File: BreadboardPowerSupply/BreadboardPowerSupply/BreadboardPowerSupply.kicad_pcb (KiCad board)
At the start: 2 copper layers, 30.5 x 52.1 mm, 15 parts, among them J1 Barrel_Jack_Switch, J2 Conn_02x02_Odd_Even, J3 Conn_02x02_Odd_Even, SW1 SW_DPDT_x2, U1 LM7805_TO220

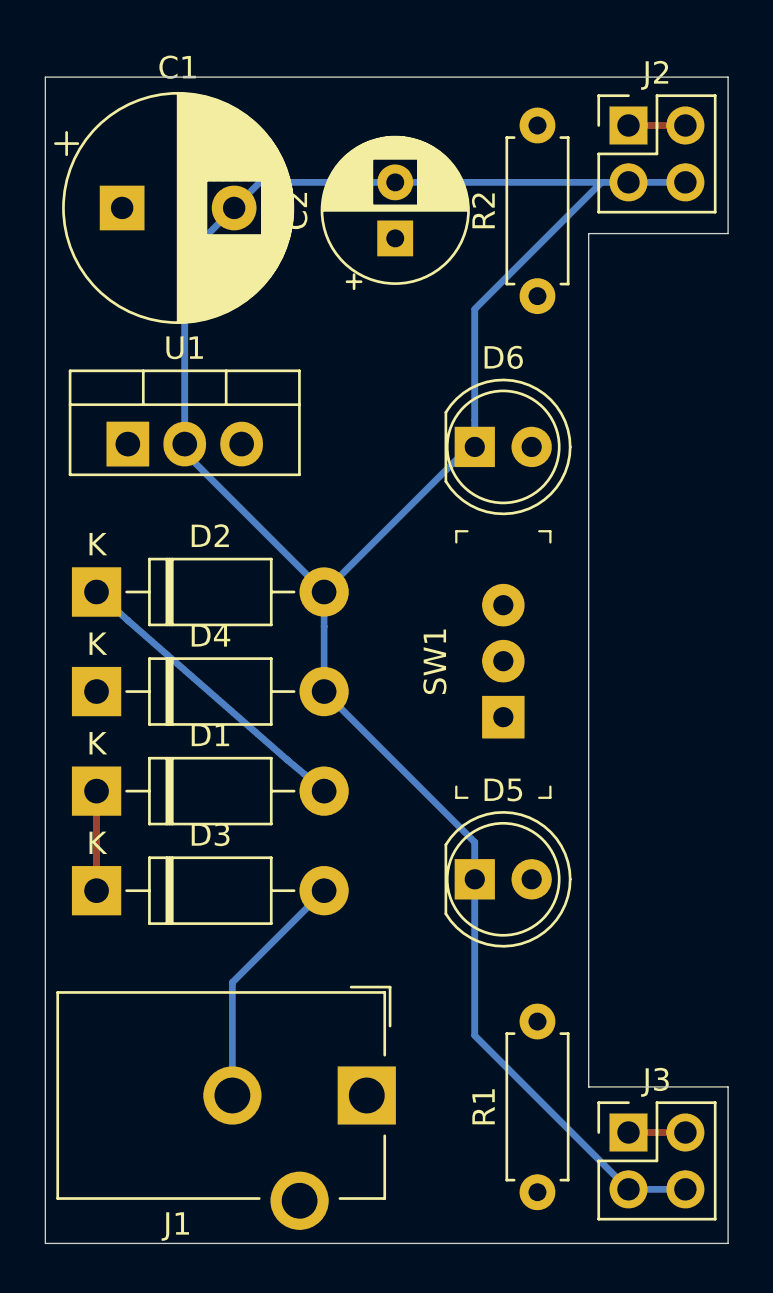
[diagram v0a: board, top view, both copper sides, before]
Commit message: start on raspberry pi hat
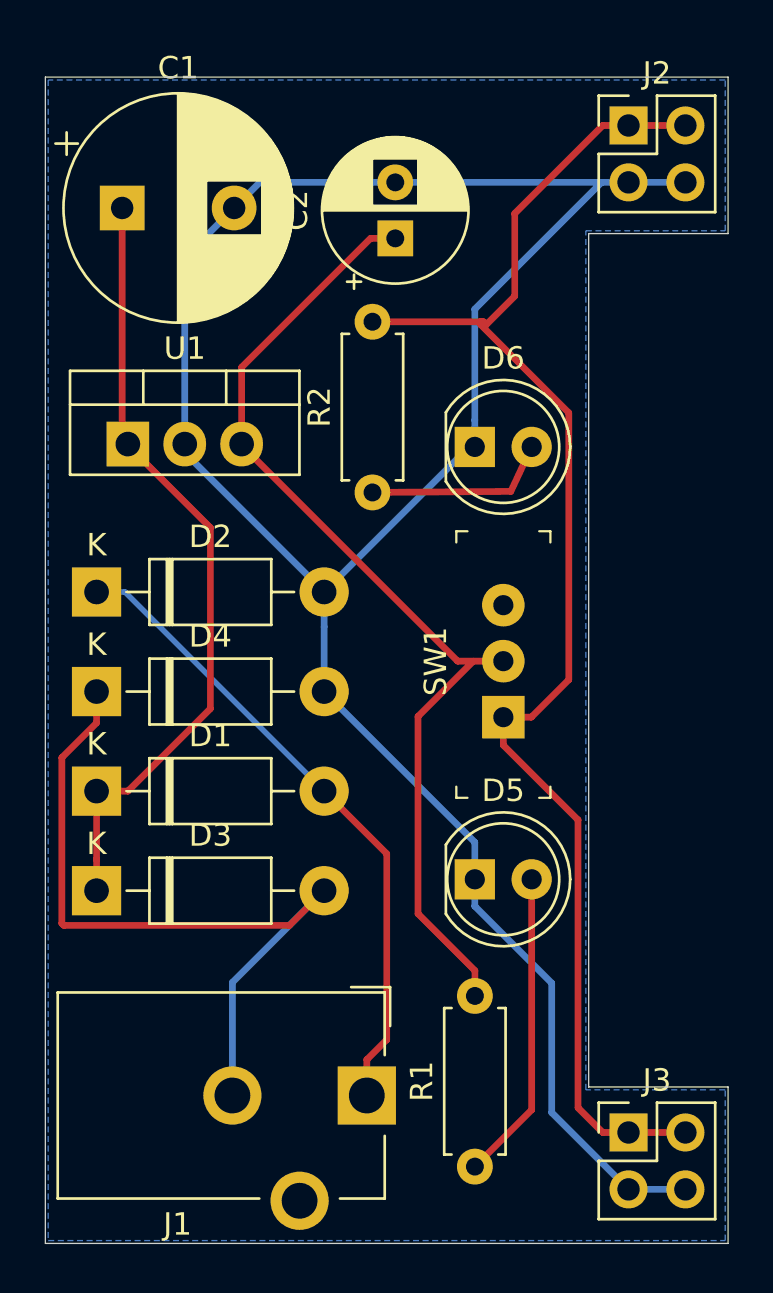
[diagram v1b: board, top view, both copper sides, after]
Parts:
- moved R2 11.4 mm to (141.2, 86.4)
- moved R1 3.02 mm to (145.8, 116.5)
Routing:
- net /Vout2: track 5.08 -> 65.2 mm
- net /Vout1: track 0.00 -> 45.4 mm
- net /Vin: track 4.45 -> 35.0 mm
- net Net-(D3-Pad2): track 10.8 -> 34.2 mm
- net Net-(D1-Pad2): track 13.5 -> 29.0 mm
- net Net-(D5-Pad2): track 0.00 -> 13.9 mm
- net Net-(D6-Pad2): track 0.00 -> 8.37 mm
- added copper zone on B.Cu, net /V-
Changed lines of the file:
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@@
     (thickness 1.6)
     (drawings 33)
-    (tracks 31)
+    (tracks 80)
     (zones 0)
     (modules 15)
@@
   )
   (setup
-    (last_trace_width 0.3)
+    (last_trace_width 0.25)
     (user_trace_width 0.3)
     (trace_clearance 0.2)
@@
     (uvia_dia 0.3)
     (uvia_drill 0.1)
-    (add_net "Net-(D1-Pad2)")
-    (add_net "Net-(D5-Pad2)")
-    (add_net "Net-(D6-Pad2)")
-    (add_net "Net-(J1-Pad3)")
-    (add_net "Net-(SW1-Pad3)")
   )
   (net_class Power ""
@@
     (add_net /Vout1)
     (add_net /Vout2)
+    (add_net "Net-(D1-Pad2)")
     (add_net "Net-(D3-Pad2)")
+    (add_net "Net-(D5-Pad2)")
+    (add_net "Net-(D6-Pad2)")
+    (add_net "Net-(J1-Pad3)")
+    (add_net "Net-(SW1-Pad3)")
   )
   (module Capacitor_THT:CP_Radial_D6.3mm_P2.50mm (layer F.Cu)
@@
   )
   (module Resistor_THT:R_Axial_DIN0207_L6.3mm_D2.5mm_P7.62mm_Horizontal (layer F.Cu)
-    (at 148.59 117.602 90)
+    (at 145.796 116.459 90)
     (descr "Resistor, Axial_DIN0207 series, Axial, Horizontal, pin pitch=7.62mm, 0.25W = 1/4W, length*diameter=6.3*2.5mm^2, http://cdn-reichelt.de/documents/datenblatt/B400/1_4W%23YAG.pdf")
     (tags "Resistor Axial_DIN0207 series Axial Horizontal pin pitch 7.62mm 0.25W = 1/4W length 6.3mm diameter 2.5mm")
@@
   )
   (module Resistor_THT:R_Axial_DIN0207_L6.3mm_D2.5mm_P7.62mm_Horizontal (layer F.Cu)
-    (at 148.59 77.597 90)
+    (at 141.224 86.36 90)
     (descr "Resistor, Axial_DIN0207 series, Axial, Horizontal, pin pitch=7.62mm, 0.25W = 1/4W, length*diameter=6.3*2.5mm^2, http://cdn-reichelt.de/documents/datenblatt/B400/1_4W%23YAG.pdf")
     (tags "Resistor Axial_DIN0207 series Axial Horizontal pin pitch 7.62mm 0.25W = 1/4W length 6.3mm diameter 2.5mm")
@@
   (segment (start 128.905 102.74) (end 128.905 99.695) (width 0.3) (layer F.Cu) (net 1))
   (segment (start 128.905 104.14) (end 128.905 102.74) (width 0.3) (layer F.Cu) (net 1))
+  (segment (start 130.305 99.695) (end 133.988 96.012) (width 0.3) (layer F.Cu) (net 1))
+  (segment (start 128.905 99.695) (end 130.305 99.695) (width 0.3) (layer F.Cu) (net 1))
+  (segment (start 130.302 84.2485) (end 130.302 84.201) (width 0.3) (layer F.Cu) (net 1))
+  (segment (start 133.988 87.9345) (end 130.302 84.2485) (width 0.3) (layer F.Cu) (net 1))
+  (segment (start 133.988 96.012) (end 133.988 87.9345) (width 0.3) (layer F.Cu) (net 1))
+  (segment (start 130.048 83.947) (end 130.302 84.201) (width 0.3) (layer F.Cu) (net 1))
+  (segment (start 130.048 73.66) (end 130.048 83.947) (width 0.3) (layer F.Cu) (net 1))
   (segment (start 155.194 117.475) (end 152.654 117.475) (width 0.3) (layer B.Cu) (net 2))
-  (segment (start 145.791 110.612) (end 145.791 103.632) (width 0.3) (layer B.Cu) (net 2))
-  (segment (start 152.654 117.475) (end 145.791 110.612) (width 0.3) (layer B.Cu) (net 2))
   (segment (start 155.194 72.517) (end 152.654 72.517) (width 0.3) (layer B.Cu) (net 2))
   (segment (start 145.791 83.128) (end 145.791 84.328) (width 0.3) (layer B.Cu) (net 2))
@@
   (segment (start 136.191 72.517) (end 142.24 72.517) (width 0.3) (layer B.Cu) (net 2))
   (segment (start 135.048 73.66) (end 136.191 72.517) (width 0.3) (layer B.Cu) (net 2))
-  (segment (start 138.176 98.933) (end 139.065 99.695) (width 0.3) (layer B.Cu) (net 4))
-  (segment (start 137.414 98.298) (end 138.176 98.933) (width 0.3) (layer B.Cu) (net 4))
-  (segment (start 128.905 90.805) (end 130.302 92.075) (width 0.3) (layer B.Cu) (net 4))
-  (segment (start 130.302 92.075) (end 137.414 98.298) (width 0.3) (layer B.Cu) (net 4))
+  (segment (start 145.791 104.832) (end 149.225 108.266) (width 0.3) (layer B.Cu) (net 2))
+  (segment (start 145.791 103.632) (end 145.791 104.832) (width 0.3) (layer B.Cu) (net 2))
+  (segment (start 149.225 114.046) (end 152.654 117.475) (width 0.3) (layer B.Cu) (net 2))
+  (segment (start 149.225 108.266) (end 149.225 114.046) (width 0.3) (layer B.Cu) (net 2))
+  (segment (start 145.796 107.70763) (end 143.256 105.16763) (width 0.3) (layer F.Cu) (net 3))
+  (segment (start 145.796 108.839) (end 145.796 107.70763) (width 0.3) (layer F.Cu) (net 3))
+  (segment (start 143.256 96.359498) (end 145.722498 93.893) (width 0.3) (layer F.Cu) (net 3))
+  (segment (start 143.256 105.16763) (end 143.256 96.359498) (width 0.3) (layer F.Cu) (net 3))
+  (segment (start 141.14 75.017) (end 142.24 75.017) (width 0.3) (layer F.Cu) (net 3))
+  (segment (start 135.382 80.775) (end 141.14 75.017) (width 0.3) (layer F.Cu) (net 3))
+  (segment (start 135.382 84.201) (end 135.382 80.775) (width 0.3) (layer F.Cu) (net 3))
+  (segment (start 145.722498 93.893) (end 147.066 93.893) (width 0.3) (layer F.Cu) (net 3))
+  (segment (start 145.0265 93.893) (end 145.722498 93.893) (width 0.3) (layer F.Cu) (net 3))
+  (segment (start 135.382 84.2485) (end 145.0265 93.893) (width 0.3) (layer F.Cu) (net 3))
+  (segment (start 135.382 84.201) (end 135.382 84.2485) (width 0.3) (layer F.Cu) (net 3))
+  (segment (start 130.175 90.805) (end 128.905 90.805) (width 0.25) (layer B.Cu) (net 4))
+  (segment (start 139.065 99.695) (end 130.175 90.805) (width 0.25) (layer B.Cu) (net 4))
+  (segment (start 140.97 111.684) (end 141.859 110.795) (width 0.3) (layer F.Cu) (net 4))
+  (segment (start 140.97 113.284) (end 140.97 111.684) (width 0.3) (layer F.Cu) (net 4))
+  (segment (start 141.859 102.489) (end 139.065 99.695) (width 0.3) (layer F.Cu) (net 4))
+  (segment (start 141.859 110.795) (end 141.859 102.489) (width 0.3) (layer F.Cu) (net 4))
   (segment (start 134.97 108.235) (end 139.065 104.14) (width 0.3) (layer B.Cu) (net 5))
   (segment (start 134.97 113.284) (end 134.97 108.235) (width 0.3) (layer B.Cu) (net 5))
+  (segment (start 128.905 96.65) (end 128.905 95.25) (width 0.3) (layer F.Cu) (net 5))
+  (segment (start 127.354999 98.200001) (end 128.905 96.65) (width 0.3) (layer F.Cu) (net 5))
+  (segment (start 127.354999 105.600001) (end 127.354999 98.200001) (width 0.3) (layer F.Cu) (net 5))
+  (segment (start 127.444999 105.690001) (end 127.354999 105.600001) (width 0.3) (layer F.Cu) (net 5))
+  (segment (start 137.514999 105.690001) (end 127.444999 105.690001) (width 0.3) (layer F.Cu) (net 5))
+  (segment (start 139.065 104.14) (end 137.514999 105.690001) (width 0.3) (layer F.Cu) (net 5))
+  (segment (start 148.331 113.924) (end 145.796 116.459) (width 0.3) (layer F.Cu) (net 6))
+  (segment (start 148.331 103.632) (end 148.331 113.924) (width 0.3) (layer F.Cu) (net 6))
+  (segment (start 147.401007 86.314007) (end 148.331 84.328) (width 0.3) (layer F.Cu) (net 7))
+  (segment (start 141.224 86.36) (end 147.401007 86.314007) (width 0.3) (layer F.Cu) (net 7))
   (segment (start 155.194 114.935) (end 152.654 114.935) (width 0.3) (layer F.Cu) (net 9))
   (segment (start 155.194 69.977) (end 152.654 69.977) (width 0.3) (layer F.Cu) (net 9))
+  (segment (start 151.504 114.935) (end 152.654 114.935) (width 0.3) (layer F.Cu) (net 9))
+  (segment (start 150.40099 113.83199) (end 151.504 114.935) (width 0.3) (layer F.Cu) (net 9))
+  (segment (start 150.40099 100.97799) (end 150.40099 113.83199) (width 0.3) (layer F.Cu) (net 9))
+  (segment (start 147.066 97.643) (end 150.40099 100.97799) (width 0.3) (layer F.Cu) (net 9))
+  (segment (start 147.066 96.393) (end 147.066 97.643) (width 0.3) (layer F.Cu) (net 9))
+  (segment (start 151.504 69.977) (end 147.574 73.907) (width 0.3) (layer F.Cu) (net 9))
+  (segment (start 152.654 69.977) (end 151.504 69.977) (width 0.3) (layer F.Cu) (net 9))
+  (segment (start 147.574 73.907) (end 147.574 77.597) (width 0.3) (layer F.Cu) (net 9))
+  (segment (start 147.574 77.597) (end 146.304 78.867) (width 0.3) (layer F.Cu) (net 9))
+  (segment (start 146.304 78.867) (end 146.177 78.74) (width 0.3) (layer F.Cu) (net 9))
+  (segment (start 148.316 96.393) (end 149.987 94.722) (width 0.3) (layer F.Cu) (net 9))
+  (segment (start 147.066 96.393) (end 148.316 96.393) (width 0.3) (layer F.Cu) (net 9))
+  (segment (start 149.987 94.722) (end 149.987 82.804) (width 0.3) (layer F.Cu) (net 9))
+  (segment (start 146.05 78.867) (end 146.05 78.74) (width 0.3) (layer F.Cu) (net 9))
+  (segment (start 149.987 82.804) (end 146.05 78.867) (width 0.3) (layer F.Cu) (net 9))
+  (segment (start 146.177 78.74) (end 146.05 78.74) (width 0.3) (layer F.Cu) (net 9))
+  (segment (start 146.05 78.74) (end 141.224 78.74) (width 0.3) (layer F.Cu) (net 9))
+  (zone (net 2) (net_name /V-) (layer B.Cu) (hatch edge 0.508)
+    (connect_pads (clearance 0.508))
+    (min_thickness 0.254)
+    (fill yes (arc_segments 32) (thermal_gap 0.508) (thermal_bridge_width 0.508))
+    (polygon
+      (pts
+        (xy 126.746 67.945) (xy 126.746 119.761) (xy 156.972 119.761) (xy 156.972 113.03) (xy 150.749 113.03)
+        (xy 150.749 74.676) (xy 156.972 74.676) (xy 156.972 67.945)
+      )
+    )
+  )
 )

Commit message: no message
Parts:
- added REF**: OSHW-Logo2_7.3x6mm_SilkScreen, Symbol:OSHW-Logo2_7.3x6mm_SilkScreen, B.Cu at (132.7, 101.1)
- added REF**: KiCad-Logo2_6mm_SilkScreen, Symbol:KiCad-Logo2_6mm_SilkScreen, B.Cu at (137.0, 79.5)
- moved D2 17.4 mm to (136.8, 106.3), turned to 90 degrees
- moved R1 14.7 mm to (148.6, 102.1), turned to 180 degrees
- moved D4 11.8 mm to (132.9, 106.3), turned to 90 degrees
- moved D3 8.00 mm to (129.0, 96.1), turned to 270 degrees
- moved D1 7.11 mm to (129.0, 92.6)
- moved D6 4.47 mm to (146.3, 79.9), turned to 270 degrees
- moved U1 3.66 mm to (131.6, 87.6), turned to 90 degrees
- moved D5 3.64 mm to (145.0, 107.2)
- moved C2 2.25 mm to (143.0, 72.9)
- moved C1 0.28 mm to (130.2, 73.9)
- moved SW1 0.28 mm to (147.3, 96.5)
- moved R2 0.28 mm to (141.0, 86.2), turned to 0 degrees
- renumbered J1 to ?, J2 to ?, J3 to ?
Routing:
- net Net-(D3-Pad2): track 34.2 -> 11.7 mm
- net /Vin: track 35.0 -> 26.3 mm
- net Net-(D5-Pad2): track 13.9 -> 5.54 mm
- net /Vout2: track 65.2 -> 59.1 mm
- net Net-(D1-Pad2): track 29.0 -> 24.4 mm
- net /V-: track 99.7 -> 95.4 mm
- net Net-(D6-Pad2): track 8.37 -> 6.92 mm
- net /Vout1: track 45.4 -> 46.5 mm
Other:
- board text added: "5V"
- board text added: "GND"
- board text added: "OFF"
- board text added: "ON"
